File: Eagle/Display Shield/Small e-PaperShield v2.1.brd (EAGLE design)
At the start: 106.3 x 56.3 mm, 118 parts, among them J2 3300060P1-ST-TF-003A, J3 2.54-8p-male-SMD, J4 2.54-8p-male-SMD, J5 2.54-6p-male-SMD, J6 2.54-6p-male-SMD, J7 2.54-2x3p-female-SMD, Q10 MOSFET-P-044021001, Q11 2N7002, Q2 2N7002, Q3 MOSFET-P-044021001, Q5 MOSFET-P-044021001, Q7 MOSFET-P-044021001, Q8 2N7002, Q9 2N7002, U2 XC6206-3.3-1300260P1, U3 74VHC125PW, U4 74VHC125PW, U5 GT20L16P1Y, U9 S-8120CNB-DRB-TF-G//200021001, X1 FH12-40S-0.5SH

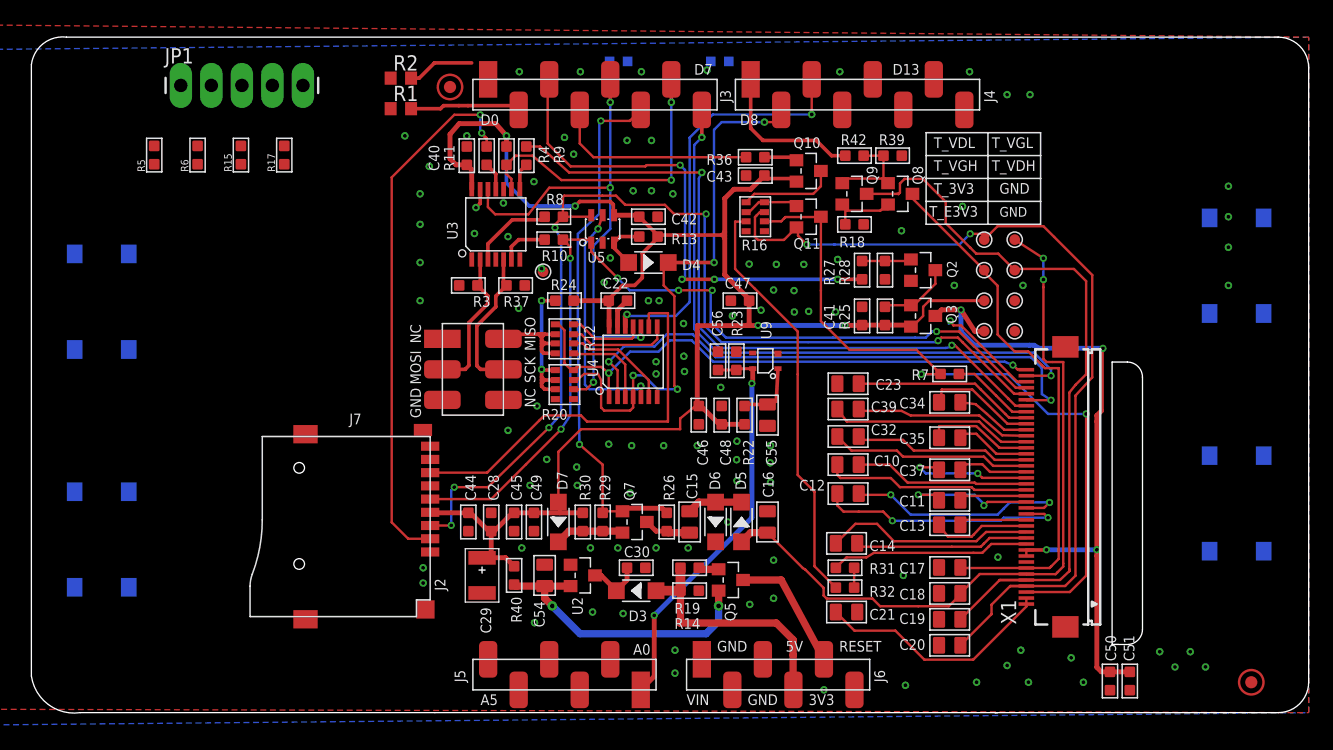
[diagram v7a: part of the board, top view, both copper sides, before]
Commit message: autorouted missing connecitons
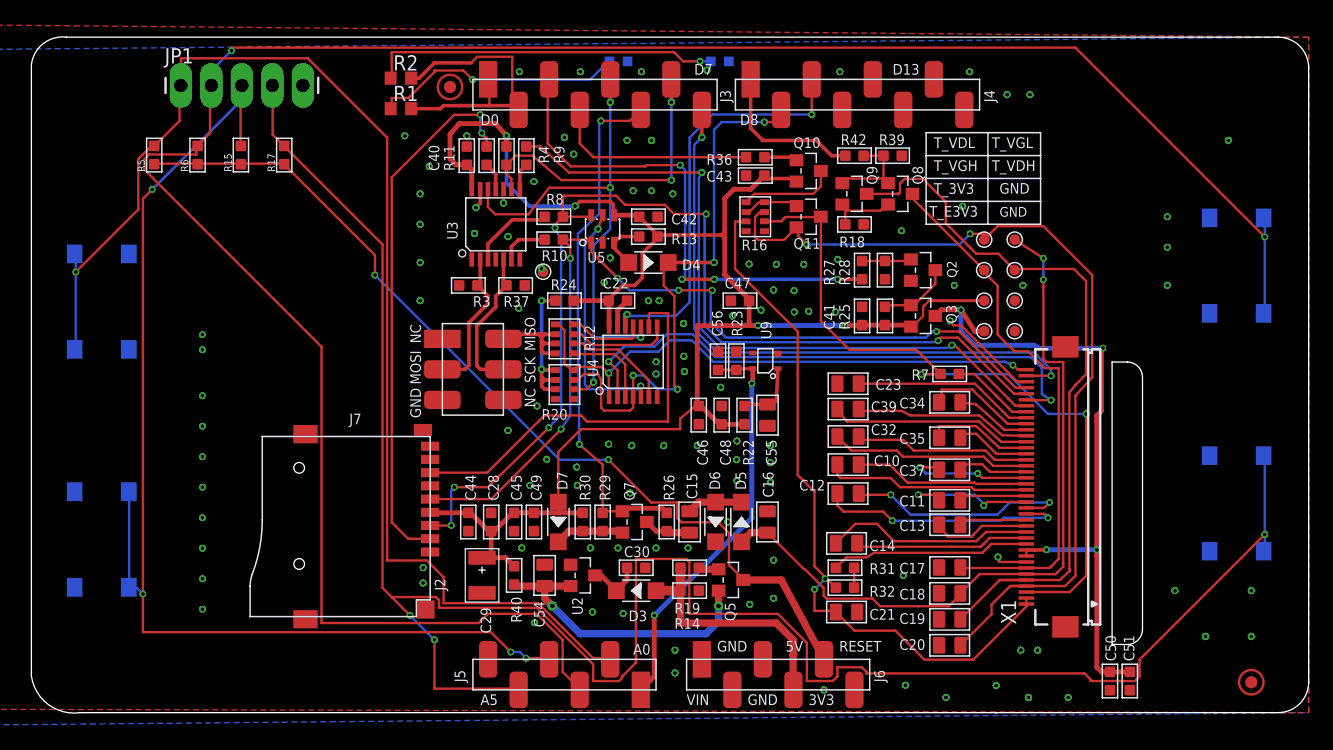
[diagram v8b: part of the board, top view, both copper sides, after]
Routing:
- net BTN1: track 0.00 -> 185.9 mm, vias 0 -> 2
- net BTN3: track 0.00 -> 172.9 mm, vias 0 -> 3
- net BTN0: track 0.00 -> 108.0 mm, vias 0 -> 1
- net BTN2: track 0.00 -> 98.5 mm, vias 0 -> 4
- net M_VCC_3V3: track 10.7 -> 77.5 mm, vias 0 -> 2
- net N$17: track 0.00 -> 29.1 mm, vias 0 -> 1
- net N$1: track 0.00 -> 21.1 mm, vias 0 -> 1
- net LED1: track 5.57 -> 13.9 mm
- net EPD_VCOM_PANEL: track 54.9 -> 59.9 mm, vias 0 -> 2
- net GND: track 12.9 -> 15.7 mm, vias 106 -> 116
- net LED0: track 8.70 -> 11.0 mm
